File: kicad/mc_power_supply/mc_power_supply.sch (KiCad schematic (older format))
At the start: 19 parts

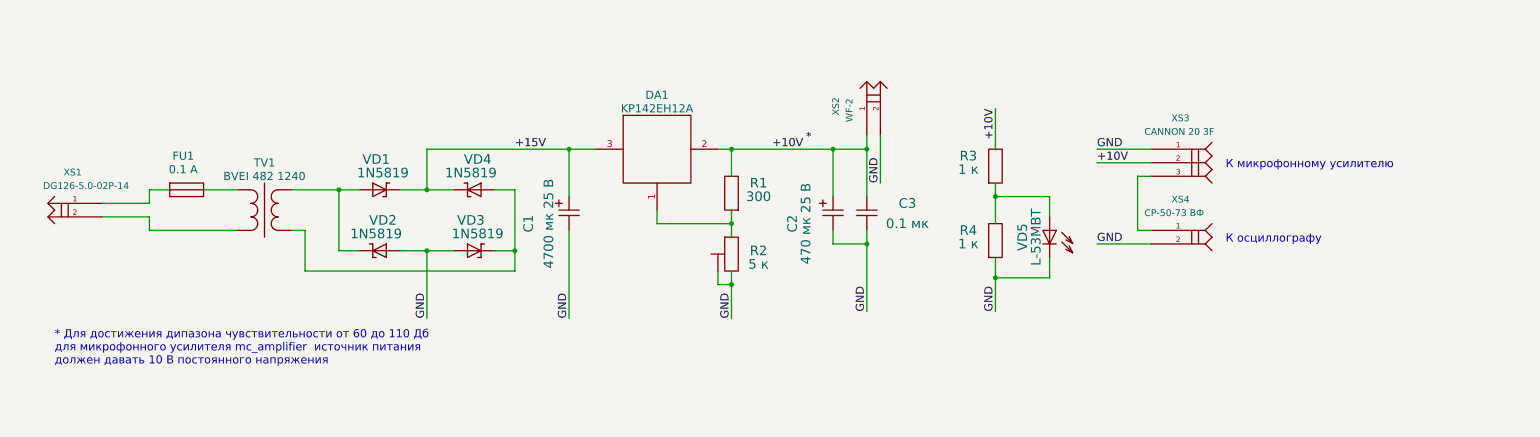
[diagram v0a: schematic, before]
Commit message: Поправил схему источника питания для микрофонного усилителя.
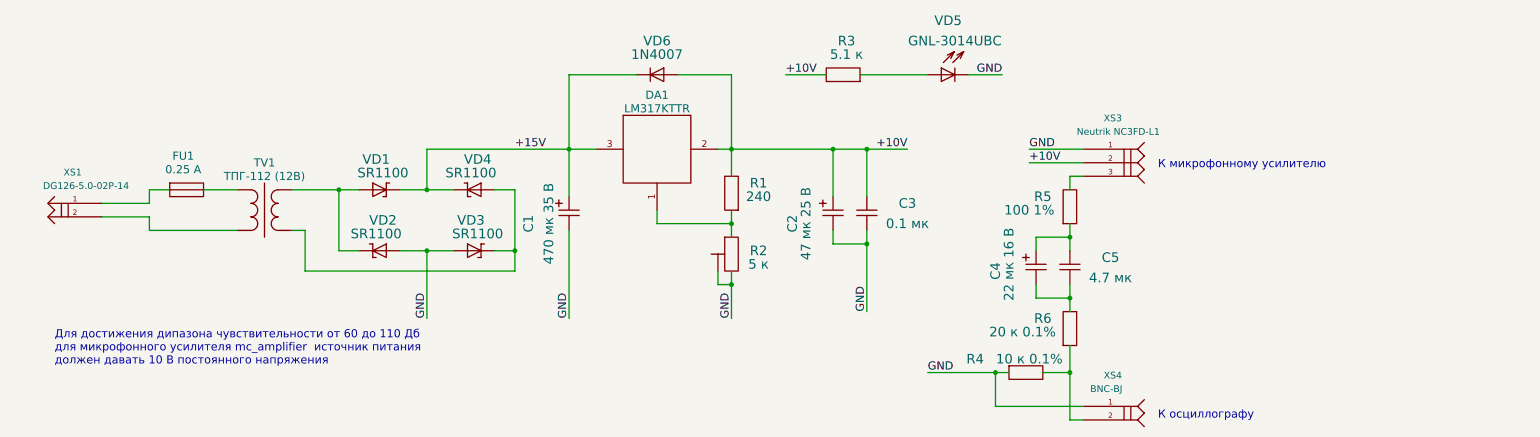
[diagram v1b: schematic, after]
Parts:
- removed XS2: WF-2, ~, symbol PIN_M_2
- added C4: 22 мк 16 В, symbol CAPITORS_ELECTROLYTIC
- added C5: 4.7 мк, symbol CAPITORS
- added R5: 100 1%, symbol RESISTOR
- added R6: 20 к 0.1%, symbol RESISTOR
- added VD6: 1N4007, symbol DIODE
- C1: value 4700 мк 25 В -> 470 мк 35 В
- C2: value 470 мк 25 В -> 47 мк 25 В
- DA1: value KP142EH12A -> LM317KTTR
- FU1: value 0.1 A -> 0.25 A
- R1: value 300 -> 240
- R3: value 1 к -> 5.1 к
- R4: value 1 к -> 10 к 0.1%
- TV1: value BVEI 482 1240 -> ТПГ-112 (12В)
- VD1, VD2, VD3, VD4: value 1N5819 -> SR1100
- VD5: value L-53MBT -> GNL-3014UBC
- XS3: value CANNON 20 3F -> Neutrik NC3FD-L1
- XS4: value СР-50-73 ВФ -> BNC-BJ
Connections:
- net +10V: now also VD6.1
- net +15V: now also VD6.2
- net GND: now also XS4.1; no longer XS4.2
- net at XS3.3: now also R5.2; no longer XS4.1
- net at R3.1, VD5.1: no longer R4.2
- new net: R4.2, R6.1, XS4.2
- new net: C4.1, C5.1, R5.1
- new net: C4.2, C5.2, R6.2
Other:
- note added: "Для достижения дипазона чувствительности от 60 до 110 Дб\nдля микрофонного усилителя mc_amplifier источник питания\nдолжен давать 10 В постоянного напряжения"
- note removed: "*"
- note removed: "* Для достижения дипазона чувствительности от 60 до 110 Дб\nдля микрофонного усилителя mc_amplifier источник питания\nдолжен давать 10 В постоянного напряжения"
- moved on the sheet: R3, VD5, XS3, XS4
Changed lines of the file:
@@
 LIBS:LFtransistor
 LIBS:mc_power_supply-cache
-EELAYER 27 0
+EELAYER 25 0
 EELAYER END
 $Descr A4 11693 8268
@@
 P 5250 2600
 F 0 "DA1" H 5500 2750 60  0000 C CNN
-F 1 "KP142EH12A" H 5500 2650 60  0000 C CNN
+F 1 "LM317KTTR" H 5500 2650 60  0000 C CNN
 F 2 "~" H 5250 2600 60  0000 C CNN
 F 3 "~" H 5250 2600 60  0000 C CNN
@@
 P 2400 3150
 F 0 "TV1" H 2600 3350 60  0000 C CNN
-F 1 "BVEI 482 1240" H 2600 3250 60  0000 C CNN
+F 1 "ТПГ-112 (12В)" H 2600 3250 60  0000 C CNN
 F 2 "" H 2400 3150 60  0000 C CNN
 F 3 "" H 2400 3150 60  0000 C CNN
@@
 P 1900 3150
 F 0 "FU1" H 2000 3400 60  0000 C CNN
-F 1 "0.1 A" H 2000 3300 60  0000 C CNN
+F 1 "0.25 A" H 2000 3300 60  0000 C CNN
 F 2 "~" H 1900 3150 60  0000 C CNN
 F 3 "~" H 1900 3150 60  0000 C CNN
@@
 P 3300 3150
 F 0 "VD1" H 3425 3375 71  0000 C CNN
-F 1 "1N5819" H 3475 3275 71  0000 C CNN
+F 1 "SR1100" H 3475 3275 71  0000 C CNN
 F 2 "" H 3300 3150 60  0000 C CNN
 F 3 "" H 3300 3150 60  0000 C CNN
@@
 P 4300 3150
 F 0 "VD4" H 4425 3375 71  0000 C CNN
-F 1 "1N5819" H 4475 3275 71  0000 C CNN
+F 1 "SR1100" H 4475 3275 71  0000 C CNN
 F 2 "" H 4300 3150 60  0000 C CNN
 F 3 "" H 4300 3150 60  0000 C CNN
@@
 P 3600 3600
 F 0 "VD2" H 3725 3825 71  0000 C CNN
-F 1 "1N5819" H 3775 3725 71  0000 C CNN
+F 1 "SR1100" H 3775 3725 71  0000 C CNN
 F 2 "" H 3600 3600 60  0000 C CNN
 F 3 "" H 3600 3600 60  0000 C CNN
@@
 P 4000 3600
 F 0 "VD3" H 4125 3825 71  0000 C CNN
-F 1 "1N5819" H 4175 3725 71  0000 C CNN
+F 1 "SR1100" H 4175 3725 71  0000 C CNN
 F 2 "" H 4000 3600 60  0000 C CNN
 F 3 "" H 4000 3600 60  0000 C CNN
@@
 P 4850 3200
 F 0 "C1" H 5050 3500 71  0000 C CNN
-F 1 "4700 мк 25 В" H 5050 3350 71  0000 C CNN
+F 1 "470 мк 35 В" H 5050 3350 71  0000 C CNN
 F 2 "" H 4850 3200 60  0000 C CNN
 F 3 "" H 4850 3200 60  0000 C CNN
@@
 	0    -1   1    0
 $EndComp
+Wire Wire Line
+	4850 2300 4850 2850
 Wire Wire Line
 	4850 2850 4850 3200
@@
 P 6050 3300
 F 0 "R1" V 6250 3500 71  0000 C CNN
-F 1 "300" V 6150 3500 71  0000 C CNN
+F 1 "240" V 6150 3500 71  0000 C CNN
 F 2 "" H 6050 3300 60  0000 C CNN
 F 3 "" H 6050 3300 60  0000 C CNN
@@
 Wire Wire Line
 	6800 2850 7050 2850
+Wire Wire Line
+	7050 2850 7350 2850
+Wire Wire Line
+	6050 2300 6050 2850
 Wire Wire Line
 	6050 2850 6050 3050
@@
 P 6800 3200
 F 0 "C2" H 7000 3500 71  0000 C CNN
-F 1 "470 мк 25 В" H 7000 3400 71  0000 C CNN
+F 1 "47 мк 25 В" H 7000 3400 71  0000 C CNN
 F 2 "" H 6800 3200 60  0000 C CNN
 F 3 "" H 6800 3200 60  0000 C CNN
@@
 Connection ~ 6050 2850
 Wire Wire Line
-	7050 2750 7050 2850
-Wire Wire Line
 	7050 2850 7050 3200
 Connection ~ 6800 2850
@@
 GND
 Connection ~ 7050 3550
-Text Label 6350 2850 0    60   ~ 0
+Text Label 7350 2850 2    60   ~ 0
 +10V
 Text Notes 1050 4450 0    60   ~ 0
-* Для достижения дипазона чувствительности от 60 до 110 Дб\nдля микрофонного усилителя mc_amplifier  источник питания\nдолжен давать 10 В постоянного напряжения
-Text Notes 6600 2800 0    60   ~ 0
-*
-$Comp
-L PIN_M_2 XS2
-U 1 1 55462B84
-P 7050 2750
-F 0 "XS2" H 7200 2950 50  0000 L BNN
-F 1 "WF-2" H 7150 2850 50  0000 L BNN
-F 2 "~" H 7500 2900 50  0001 C CNN
-F 3 "" H 7050 2750 60  0000 C CNN
-	1    7050 2750
-	0    -1   -1   0
-$EndComp
+Для достижения дипазона чувствительности от 60 до 110 Дб\nдля микрофонного усилителя mc_amplifier  источник питания\nдолжен давать 10 В постоянного напряжения
 Connection ~ 7050 2850
-Text Label 7150 3100 1    60   ~ 0
-GND
-Wire Wire Line
-	7150 2750 7150 3100
 $Comp
 L PIN_F_3 XS3
 U 1 1 55462C0D
-P 9150 2850
-F 0 "XS3" H 9300 3050 50  0000 L BNN
-F 1 "CANNON 20 3F" H 9100 2950 50  0000 L BNN
-F 2 "~" H 9600 3000 50  0001 C CNN
-F 3 "" H 9150 2850 60  0000 C CNN
-	1    9150 2850
-	1    0    0    -1
-$EndComp
-Text Label 8750 2950 0    60   ~ 0
+P 8650 2850
+F 0 "XS3" H 8800 3050 50  0000 L BNN
+F 1 "Neutrik NC3FD-L1" H 8600 2950 50  0000 L BNN
+F 2 "~" H 9100 3000 50  0001 C CNN
+F 3 "" H 8650 2850 60  0000 C CNN
+	1    8650 2850
+	1    0    0    -1
+$EndComp
+Text Label 8250 2950 0    60   ~ 0
 +10V
 Wire Wire Line
-	8750 2950 9150 2950
-Wire Wire Line
-	9150 2850 8750 2850
-Text Label 8750 2850 0    60   ~ 0
+	8250 2950 8650 2950
+Wire Wire Line
+	8650 2850 8250 2850
+Text Label 8250 2850 0    60   ~ 0
 GND
 $Comp
 L PIN_F_2 XS4
 U 1 1 55462D16
-P 9150 3450
-F 0 "XS4" H 9300 3650 50  0000 L BNN
-F 1 "СР-50-73 ВФ" H 9100 3550 50  0000 L BNN
-F 2 "~" H 9600 3600 50  0001 C CNN
-F 3 "" H 9150 3450 60  0000 C CNN
-	1    9150 3450
-	1    0    0    -1
-$EndComp
-Text Label 8750 3550 0    60   ~ 0
-GND
-Wire Wire Line
-	8750 3550 9150 3550
-Wire Wire Line
-	9150 3050 9050 3050
-Wire Wire Line
-	9050 3050 9050 3450
-Wire Wire Line
-	9050 3450 9150 3450
-Text Notes 9700 3000 0    60   ~ 0
+P 8650 4750
+F 0 "XS4" H 8800 4950 50  0000 L BNN
+F 1 "BNC-BJ" H 8700 4850 50  0000 L BNN
+F 2 "~" H 9100 4900 50  0001 C CNN
+F 3 "" H 8650 4750 60  0000 C CNN
+	1    8650 4750
+	1    0    0    -1
+$EndComp
+Wire Wire Line
+	8650 3050 8550 3050
+Text Notes 9200 3000 0    60   ~ 0
 К микрофонному усилителю
-Text Notes 9700 3550 0    60   ~ 0
+Text Notes 9200 4850 0    60   ~ 0
 К осциллографу
 $Comp
 L DIODE_LIGHT VD5
 U 1 1 55462DB4
-P 8400 3350
-F 0 "VD5" H 8550 3150 71  0000 C CNN
-F 1 "L-53MBT" H 8550 3250 71  0000 C CNN
-F 2 "" H 8400 3350 60  0000 C CNN
-F 3 "" H 8400 3350 60  0000 C CNN
-	1    8400 3350
-	0    1    1    0
-$EndComp
-$Comp
-L RESISTOR R4
-U 1 1 55462DEE
-P 8000 3650
-F 0 "R4" V 8200 3850 71  0000 C CNN
-F 1 "1 к" V 8100 3850 71  0000 C CNN
-F 2 "" H 8000 3650 60  0000 C CNN
-F 3 "" H 8000 3650 60  0000 C CNN
-	1    8000 3650
-	0    -1   -1   0
+P 7500 2300
+F 0 "VD5" H 7650 2700 71  0000 C CNN
+F 1 "GNL-3014UBC" H 7700 2550 71  0000 C CNN
+F 2 "" H 7500 2300 60  0000 C CNN
+F 3 "" H 7500 2300 60  0000 C CNN
+	1    7500 2300
+	1    0    0    -1
 $EndComp
 $Comp
 L RESISTOR R3
 U 1 1 55462DFE
-P 8000 3100
-F 0 "R3" V 8200 3300 71  0000 C CNN
-F 1 "1 к" V 8100 3300 71  0000 C CNN
-F 2 "" H 8000 3100 60  0000 C CNN
-F 3 "" H 8000 3100 60  0000 C CNN
-	1    8000 3100
+P 7000 2300
+F 0 "R3" H 7100 2050 71  0000 C CNN
+F 1 "5.1 к" H 7100 2150 71  0000 C CNN
+F 2 "" H 7000 2300 60  0000 C CNN
+F 3 "" H 7000 2300 60  0000 C CNN
+	1    7000 2300
+	-1   0    0    1
+$EndComp
+Wire Wire Line
+	7000 2300 7500 2300
+Wire Wire Line
+	7800 2300 8050 2300
+Text Label 8050 2300 2    60   ~ 0
+GND
+Wire Wire Line
+	6750 2300 6450 2300
+Text Label 6450 2300 0    60   ~ 0
++10V
+$Comp
+L RESISTOR R5
+U 1 1 5AAE9602
+P 8550 3400
+F 0 "R5" V 8750 3600 71  0000 C CNN
+F 1 "100 1%" V 8650 3700 71  0000 C CNN
+F 2 "" H 8550 3400 60  0000 C CNN
+F 3 "" H 8550 3400 60  0000 C CNN
+	1    8550 3400
 	0    -1   -1   0
 $EndComp
-Wire Wire Line
-	8000 3100 8000 3200
-Wire Wire Line
-	8000 3200 8000 3400
-Wire Wire Line
-	8000 3200 8400 3200
-Connection ~ 8000 3200
-Wire Wire Line
-	8400 3200 8400 3350
-Wire Wire Line
-	8000 3650 8000 3800
-Wire Wire Line
-	8000 3800 8000 4050
-Wire Wire Line
-	8000 3800 8400 3800
-Wire Wire Line
-	8400 3800 8400 3650
-Text Label 8000 4050 1    60   ~ 0
-GND
-Connection ~ 8000 3800
-Wire Wire Line
-	8000 2850 8000 2550
-Text Label 8000 2550 3    60   ~ 0
-+10V
+$Comp
+L CAPITORS C5
+U 1 1 5AAE9671
+P 8550 3600
+F 0 "C5" V 8600 3300 71  0000 C CNN
+F 1 "4.7 мк" V 8750 3300 71  0000 C CNN
+F 2 "" H 8550 3600 60  0000 C CNN
+F 3 "" H 8550 3600 60  0000 C CNN
+	1    8550 3600
+	0    -1   1    0
+$EndComp
+$Comp
+L CAPITORS_ELECTROLYTIC C4
+U 1 1 5AAE96FB
+P 8300 3600
+F 0 "C4" H 8450 3900 71  0000 C CNN
+F 1 "22 мк 16 В" H 8400 3800 71  0000 C CNN
+F 2 "" H 8300 3600 60  0000 C CNN
+F 3 "" H 8300 3600 60  0000 C CNN
+	1    8300 3600
+	0    -1   1    0
+$EndComp
+Wire Wire Line
+	8550 3050 8550 3150
+Wire Wire Line
+	8300 3600 8300 3500
+Wire Wire Line
+	8300 3500 8550 3500
+Wire Wire Line
+	8550 3400 8550 3500
+Wire Wire Line
+	8550 3500 8550 3600
+Connection ~ 8550 3500
+Wire Wire Line
+	8300 3850 8300 3950
+Wire Wire Line
+	8300 3950 8550 3950
+Wire Wire Line
+	8550 3850 8550 3950
+Wire Wire Line
+	8550 3950 8550 4050
+$Comp
+L RESISTOR R6
+U 1 1 5AAE9BFC
+P 8550 4300
+F 0 "R6" V 8750 4500 71  0000 C CNN
+F 1 "20 к 0.1%" V 8650 4650 71  0000 C CNN
+F 2 "" H 8550 4300 60  0000 C CNN
+F 3 "" H 8550 4300 60  0000 C CNN
+	1    8550 4300
+	0    -1   -1   0
+$EndComp
+$Comp
+L RESISTOR R4
+U 1 1 5AAE9C52
+P 8100 4500
+F 0 "R4" H 7850 4600 71  0000 C CNN
+F 1 "10 к 0.1%" H 8250 4600 71  0000 C CNN
+F 2 "" H 8100 4500 60  0000 C CNN
+F 3 "" H 8100 4500 60  0000 C CNN
+	1    8100 4500
+	1    0    0    -1
+$EndComp
+Wire Wire Line
+	8350 4500 8550 4500
+Wire Wire Line
+	8550 4300 8550 4500
+Wire Wire Line
+	8550 4500 8550 4850
+Connection ~ 8550 3950
+Wire Wire Line
+	8550 4850 8650 4850
+Connection ~ 8550 4500
+Text Label 7500 4500 0    60   ~ 0
+GND
+Wire Wire Line
+	7500 4500 8000 4500
+Wire Wire Line
+	8000 4500 8100 4500
+Wire Wire Line
+	8000 4500 8000 4750
+Wire Wire Line
+	8000 4750 8650 4750
+Connection ~ 8000 4500
+$Comp
+L DIODE VD6
+U 1 1 5AAEB4B2
+P 5650 2300
+F 0 "VD6" H 5800 2550 71  0000 C CNN
+F 1 "1N4007" H 5800 2450 71  0000 C CNN
+F 2 "" H 5650 2300 60  0000 C CNN
+F 3 "" H 5650 2300 60  0000 C CNN
+	1    5650 2300
+	-1   0    0    -1
+$EndComp
+Wire Wire Line
+	4850 2300 5350 2300
+Wire Wire Line
+	5650 2300 6050 2300
 $EndSCHEMATC

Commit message: Поравил схему источника питания микрофона.
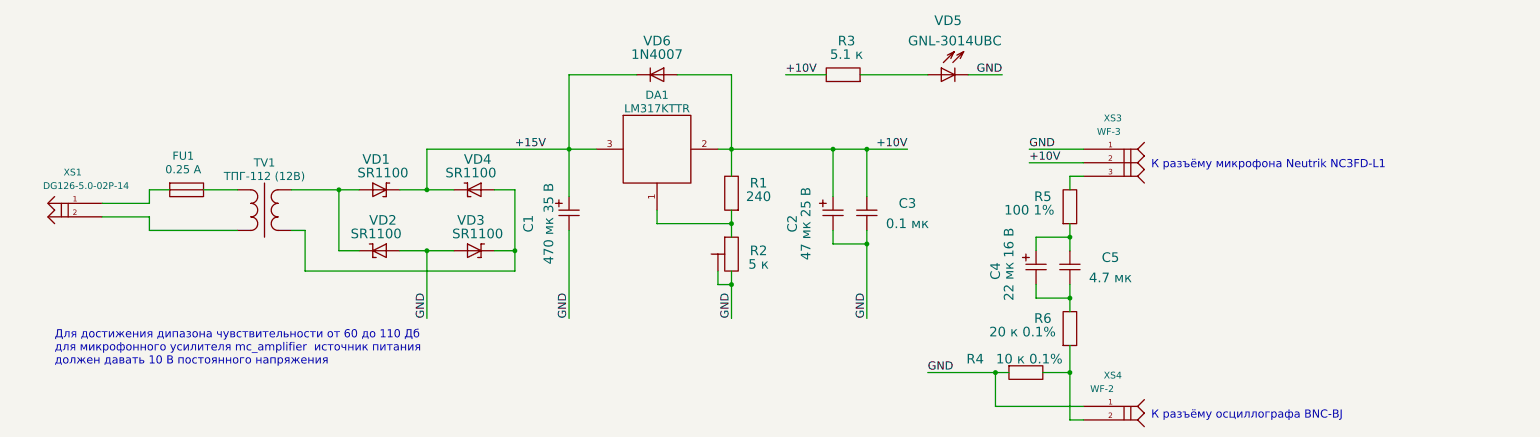
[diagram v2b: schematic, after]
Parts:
- XS3: value Neutrik NC3FD-L1 -> WF-3
- XS4: value BNC-BJ -> WF-2
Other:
- note added: "К разъёму микрофона Neutrik NC3FD-L1"
- note added: "К разъёму осциллографа BNC-BJ"
- note removed: "К микрофонному усилителю"
- note removed: "К осциллографу"
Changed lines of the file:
@@
 	7050 3450 7050 3550
 Wire Wire Line
-	7050 3550 7050 4050
-Text Label 7050 4050 1    60   ~ 0
+	7050 3550 7050 4100
+Text Label 7050 4100 1    60   ~ 0
 GND
 Connection ~ 7050 3550
@@
 P 8650 2850
 F 0 "XS3" H 8800 3050 50  0000 L BNN
-F 1 "Neutrik NC3FD-L1" H 8600 2950 50  0000 L BNN
+F 1 "WF-3" H 8750 2950 50  0000 L BNN
 F 2 "~" H 9100 3000 50  0001 C CNN
 F 3 "" H 8650 2850 60  0000 C CNN
@@
 P 8650 4750
 F 0 "XS4" H 8800 4950 50  0000 L BNN
-F 1 "BNC-BJ" H 8700 4850 50  0000 L BNN
+F 1 "WF-2" H 8700 4850 50  0000 L BNN
 F 2 "~" H 9100 4900 50  0001 C CNN
 F 3 "" H 8650 4750 60  0000 C CNN
@@
 Wire Wire Line
 	8650 3050 8550 3050
-Text Notes 9200 3000 0    60   ~ 0
-К микрофонному усилителю
-Text Notes 9200 4850 0    60   ~ 0
-К осциллографу
+Text Notes 9150 3000 0    60   ~ 0
+К разъёму микрофона Neutrik NC3FD-L1
+Text Notes 9150 4850 0    60   ~ 0
+К разъёму осциллографа BNC-BJ
 $Comp
 L DIODE_LIGHT VD5
